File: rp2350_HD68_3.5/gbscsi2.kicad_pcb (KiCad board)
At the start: 4 copper layers, 100 x 93.5 mm, 170 parts, among them J1 USB_DATA, J2 TF003, J3 Conn_01x02, J4 MnL, J5 HD68, J6 Conn_01x05, J7 Conn_01x04, J8 Conn_01x02, Q1 AO3401A, Q10 AO3401A, Q11 AO3401A, Q12 AO3401A, Q13 AO3401A, Q14 AO3401A, Q15 AO3401A, Q16 AO3401A, Q17 AO3401A, Q18 AO3401A, Q19 AO3401A, Q2 AO3401A, Q20 AO3401A, Q21 AO3401A, Q22 AO3401A, Q23 AO3401A, Q24 AO3401A, Q25 AO3401A, Q26 AO3401A, Q27 AO3401A, Q3 AO3401A, Q4 AO3401A, Q5 AO3401A, Q6 AO3401A, Q7 AO3401A, Q8 AO3401A, Q9 AO3401A, SW1 SW_DIP_x04, U1 RP2350_80QFN, U10 W25Q128JVS, U11 74LVT245, U2 74LVT245, U3 74LVT245, U4 74LVT125, U5 74LVT125, U6 74LVT125, U7 AZ1117-2.85, U8 AP62250WU, U9 USB TVS, Y1 12MHz

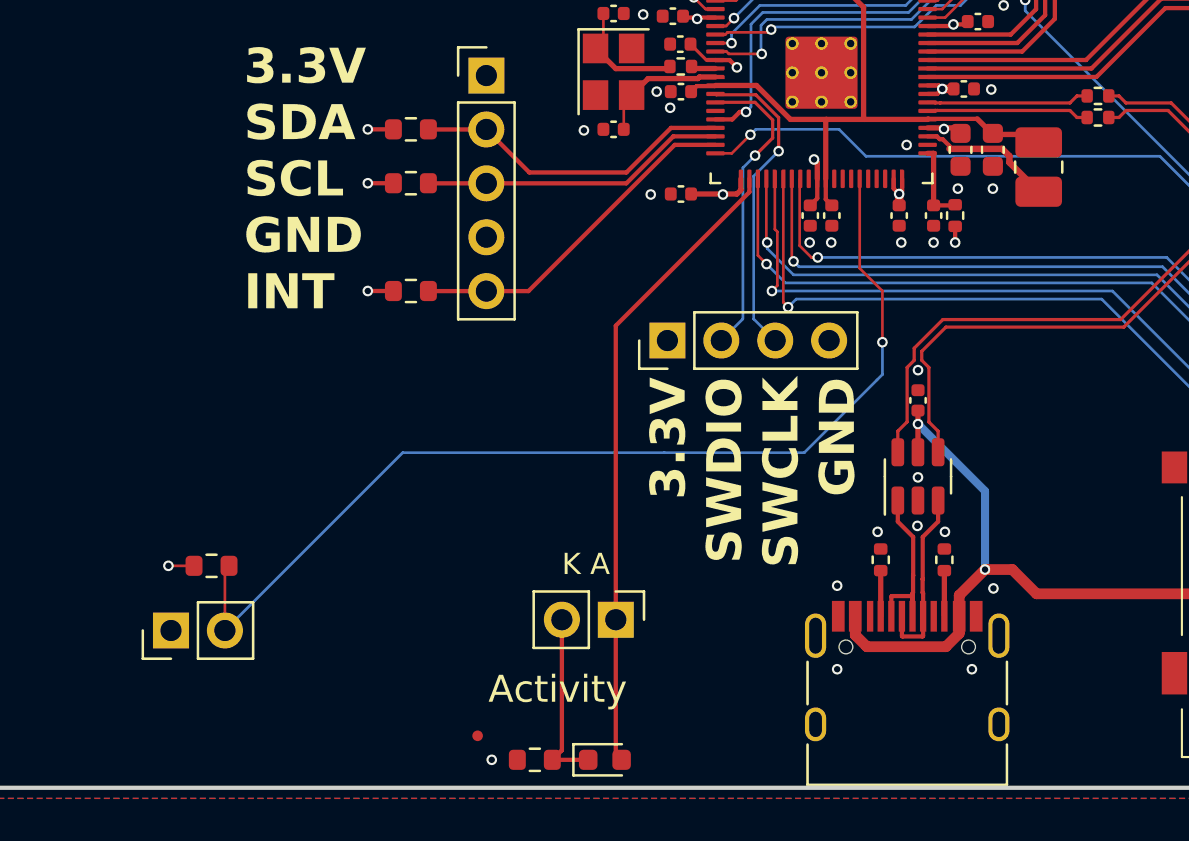
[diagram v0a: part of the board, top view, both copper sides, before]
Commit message: Minor BoM fixes, added left-behind HD68 variant eject switch
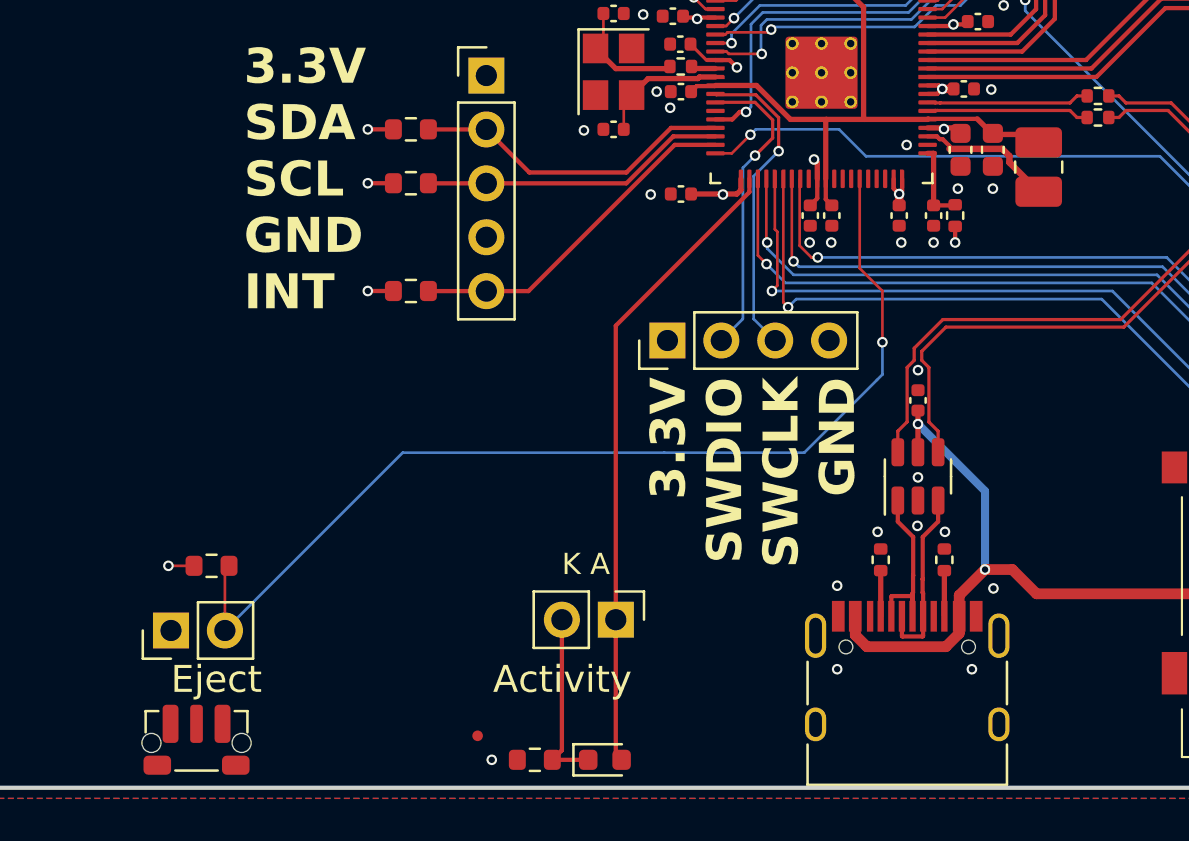
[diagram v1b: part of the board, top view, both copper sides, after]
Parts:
- added SW2: GT-TC108A-H034-L1S, GBSCSI:SW_Push_1P1T-MP_NO_Horizontal_Alps_SKRTLAE010, F.Cu at (44.3, 134.6)
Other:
- board text added: "Eject"
